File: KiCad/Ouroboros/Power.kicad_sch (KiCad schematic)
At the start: 8 parts, among them J2 Jack-DC, U1 Opamp_Quad, U3 LM78L05_TO92

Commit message: Updating schematic
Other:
- note added: "DC IN"
- note added: "[4] Power"
- moved on the sheet: C4, C5, C6, C7, J2, U3

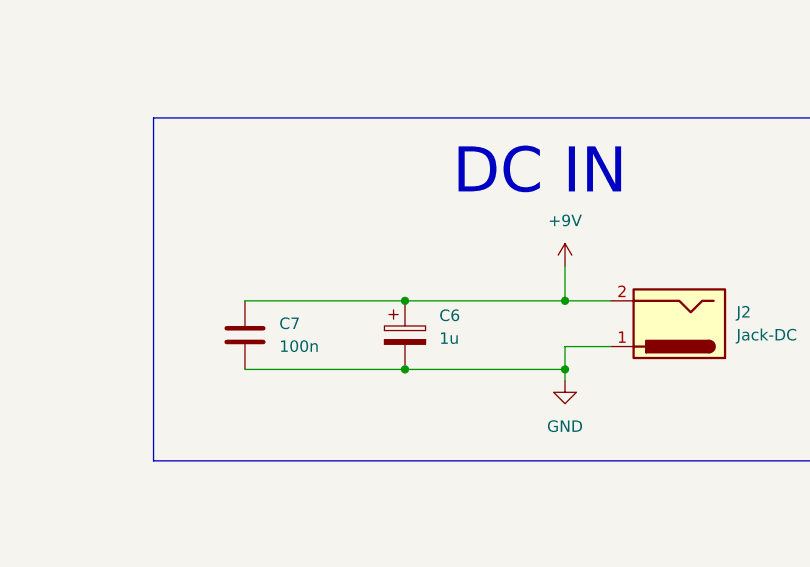
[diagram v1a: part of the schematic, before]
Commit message: Linking nets
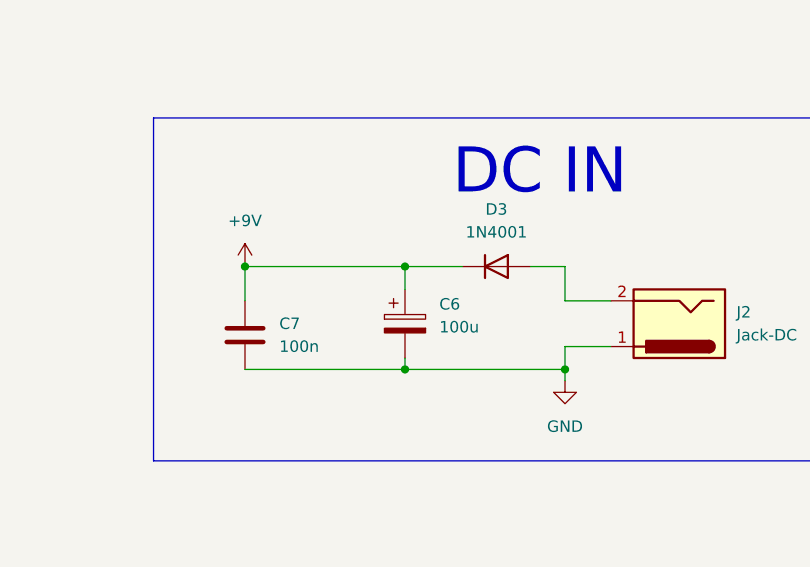
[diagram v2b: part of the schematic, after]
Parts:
- added D3: 1N4001, Diode_THT:D_DO-41_SOD81_P10.16mm_Horizontal, symbol Diode:1N4001
- C6: value 1u -> 100u
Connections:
- net +9V: now also D3.1 (K); no longer J2.2
- new net: D3.2 (A), J2.2
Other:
- moved on the sheet: C6
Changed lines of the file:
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@@
 	)
 	(junction
-		(at 134.62 63.5)
+		(at 116.84 59.69)
 		(diameter 0)
 		(color 0 0 0 0)
@@
 	)
 	(junction
-		(at 152.4 63.5)
-		(diameter 0)
-		(color 0 0 0 0)
-	)
-	(junction
 		(at 128.27 125.73)
 		(diameter 0)
@@
 		(color 0 0 0 0)
 	)
+	(junction
+		(at 134.62 59.69)
+		(diameter 0)
+		(color 0 0 0 0)
+	)
 	(polyline
 		(pts
@@
 	(wire
 		(pts
+			(xy 134.62 59.69) (xy 134.62 62.23)
+		)
+		(stroke
+			(width 0)
+			(type default)
+		)
+	)
+	(wire
+		(pts
 			(xy 54.61 93.98) (xy 54.61 99.06)
 		)
@@
 		)
 	)
+	(wire
+		(pts
+			(xy 148.59 59.69) (xy 152.4 59.69)
+		)
+		(stroke
+			(width 0)
+			(type default)
+		)
+	)
 	(polyline
 		(pts
@@
 	(wire
 		(pts
-			(xy 134.62 63.5) (xy 152.4 63.5)
-		)
-		(stroke
-			(width 0)
-			(type default)
-		)
-	)
-	(wire
-		(pts
 			(xy 74.93 99.06) (xy 74.93 101.6)
 		)
@@
 	(wire
 		(pts
+			(xy 134.62 69.85) (xy 134.62 71.12)
+		)
+		(stroke
+			(width 0)
+			(type default)
+		)
+	)
+	(wire
+		(pts
 			(xy 152.4 71.12) (xy 152.4 68.58)
 		)
@@
 		)
 	)
+	(wire
+		(pts
+			(xy 134.62 71.12) (xy 152.4 71.12)
+		)
+		(stroke
+			(width 0)
+			(type default)
+		)
+	)
 	(polyline
 		(pts
@@
 	(wire
 		(pts
+			(xy 134.62 59.69) (xy 140.97 59.69)
+		)
+		(stroke
+			(width 0)
+			(type default)
+		)
+	)
+	(wire
+		(pts
 			(xy 152.4 125.73) (xy 167.64 125.73)
 		)
@@
 	(wire
 		(pts
+			(xy 116.84 59.69) (xy 116.84 63.5)
+		)
+		(stroke
+			(width 0)
+			(type default)
+		)
+	)
+	(wire
+		(pts
 			(xy 128.27 125.73) (xy 137.16 125.73)
 		)
@@
 	(wire
 		(pts
-			(xy 134.62 71.12) (xy 152.4 71.12)
-		)
-		(stroke
-			(width 0)
-			(type default)
-		)
-	)
-	(wire
-		(pts
-			(xy 116.84 63.5) (xy 134.62 63.5)
+			(xy 116.84 59.69) (xy 134.62 59.69)
 		)
 		(stroke
@@
 	(symbol
 		(lib_id "Device:C_Polarized")
-		(at 134.62 67.31 0)
+		(at 134.62 66.04 0)
 		(unit 1)
 		(exclude_from_sim no)
@@
 		(fields_autoplaced yes)
 		(property "Reference" "C6"
-			(at 138.43 65.1509 0)
+			(at 138.43 63.8809 0)
 			(effects
 				(font
@@
 			)
 		)
-		(property "Value" "1u"
-			(at 138.43 67.6909 0)
+		(property "Value" "100u"
+			(at 138.43 66.4209 0)
 			(effects
 				(font
@@
 		)
 		(property "Footprint" ""
-			(at 135.5852 71.12 0)
+			(at 135.5852 69.85 0)
 			(effects
 				(font
@@
 		)
 		(property "Datasheet" "~"
-			(at 134.62 67.31 0)
+			(at 134.62 66.04 0)
 			(effects
 				(font
@@
 		)
 		(property "Description" "Polarized capacitor"
-			(at 134.62 67.31 0)
+			(at 134.62 66.04 0)
 			(effects
 				(font
@@
 	(symbol
 		(lib_id "power:+9V")
-		(at 152.4 59.69 0)
+		(at 116.84 59.69 0)
 		(unit 1)
 		(exclude_from_sim no)
@@
 		(fields_autoplaced yes)
 		(property "Reference" "#PWR08"
-			(at 152.4 63.5 0)
+			(at 116.84 63.5 0)
 			(effects
 				(font
@@
 		)
 		(property "Value" "+9V"
-			(at 152.4 54.61 0)
+			(at 116.84 54.61 0)
 			(effects
 				(font
@@
 		)
 		(property "Footprint" ""
-			(at 152.4 59.69 0)
+			(at 116.84 59.69 0)
 			(effects
 				(font
@@
 		)
 		(property "Datasheet" ""
-			(at 152.4 59.69 0)
+			(at 116.84 59.69 0)
 			(effects
 				(font
@@
 		)
 		(property "Description" "Power symbol creates a global label with name \"+9V\""
-			(at 152.4 59.69 0)
+			(at 116.84 59.69 0)
 			(effects
 				(font
@@
 					(unit 1)
 				)
+			)
+		)
+	)
+	(symbol
+		(lib_id "Diode:1N4001")
+		(at 144.78 59.69 0)
+		(unit 1)
+		(exclude_from_sim no)
+		(in_bom yes)
+		(on_board yes)
+		(dnp no)
+		(fields_autoplaced yes)
+		(property "Reference" "D3"
+			(at 144.78 53.34 0)
+			(effects
+				(font
+					(size 1.27 1.27)
+				)
+			)
+		)
+		(property "Value" "1N4001"
+			(at 144.78 55.88 0)
+			(effects
+				(font
+					(size 1.27 1.27)
+				)
+			)
+		)
+		(property "Footprint" "Diode_THT:D_DO-41_SOD81_P10.16mm_Horizontal"
+			(at 144.78 59.69 0)
+			(effects
+				(font
+					(size 1.27 1.27)
+				)
+				(hide yes)
+			)
+		)
+		(property "Datasheet" "http://www.vishay.com/docs/88503/1n4001.pdf"
+			(at 144.78 59.69 0)
+			(effects
+				(font
+					(size 1.27 1.27)
+				)
+				(hide yes)
+			)
+		)
+		(property "Description" "50V 1A General Purpose Rectifier Diode, DO-41"
+			(at 144.78 59.69 0)
+			(effects
+				(font
+					(size 1.27 1.27)
+				)
+				(hide yes)
+			)
+		)
+		(property "Sim.Device" "D"
+			(at 144.78 59.69 0)
+			(effects
+				(font
+					(size 1.27 1.27)
+				)
+				(hide yes)
+			)
+		)
+		(property "Sim.Pins" "1=K 2=A"
+			(at 144.78 59.69 0)
+			(effects
+				(font
+					(size 1.27 1.27)
+				)
+				(hide yes)
+			)
+		)
+		(pin "2"
+		)
+		(pin "1"
+		)
+		(instances
+			(project ""
+				(path "/a2662f7c-8239-40ad-828c-dd886b1cb258/62d72753-1043-42a5-8194-984b7e294543"
+					(reference "D3")
+					(unit 1)
+				)

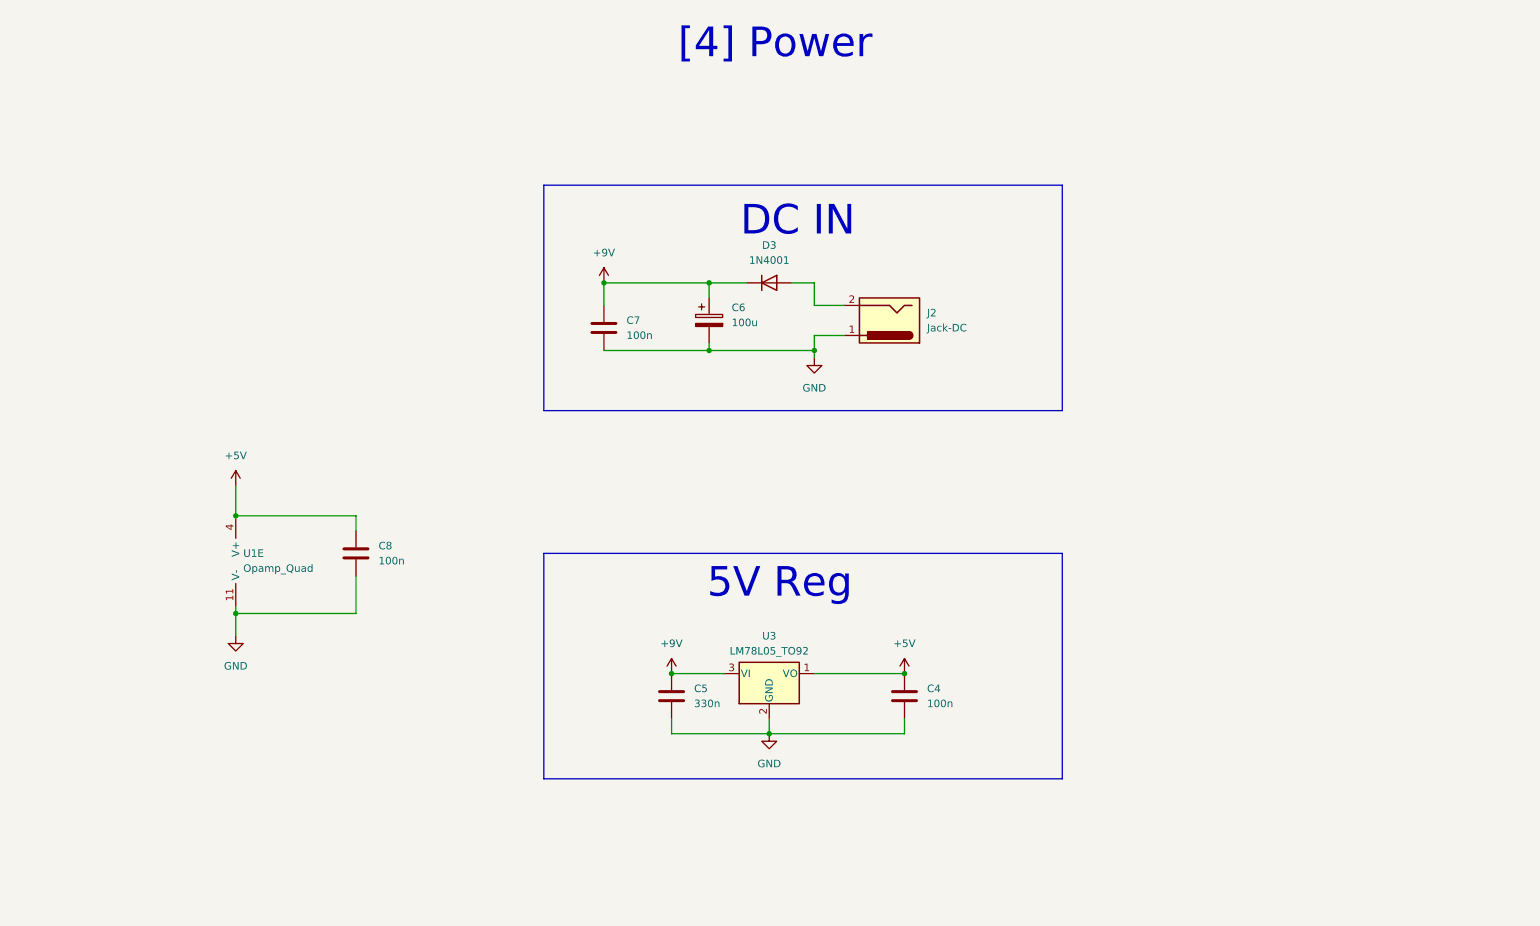
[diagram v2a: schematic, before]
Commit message: Updated schematic, started PCB
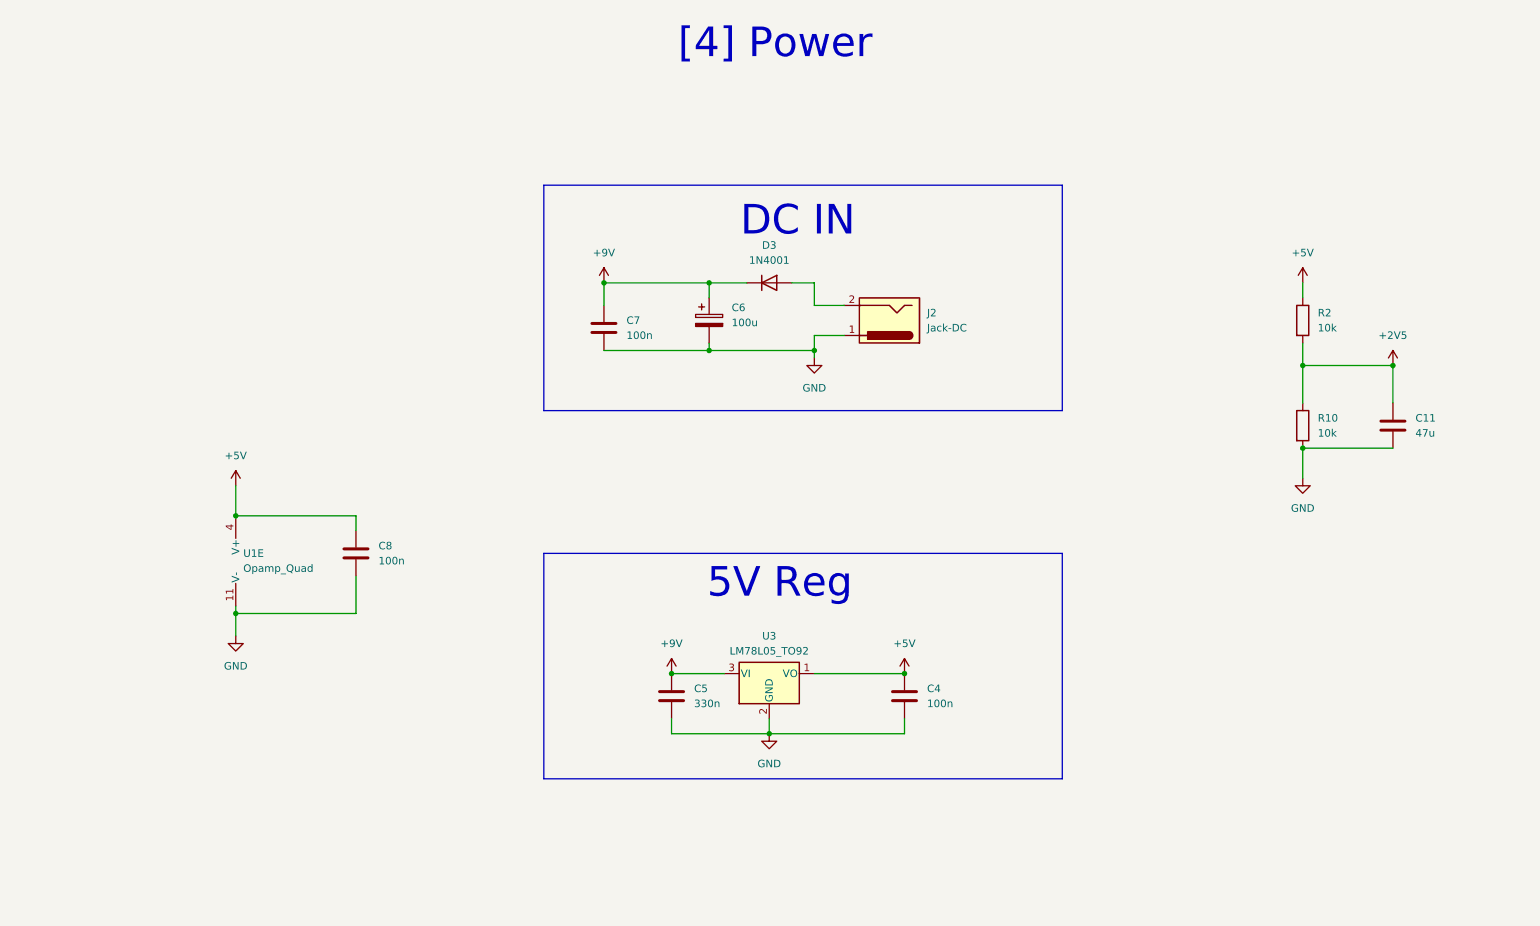
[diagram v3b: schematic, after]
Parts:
- added C11: 47u, Capacitor_THT:C_Rect_L7.0mm_W3.5mm_P5.00mm, symbol Device:C
- added R10, R2: 10k, Resistor_THT:R_Axial_DIN0207_L6.3mm_D2.5mm_P10.16mm_Horizontal, symbol Device:R
- C4, C5, C7, C8: footprint (none) -> Capacitor_THT:C_Rect_L7.0mm_W3.5mm_P5.00mm
- C6: footprint (none) -> Capacitor_THT:CP_Radial_D5.0mm_P2.50mm
- J2: footprint (none) -> Connector_BarrelJack:BarrelJack_CUI_PJ-063AH_Horizontal_CircularHoles
- U1: footprint (none) -> Package_DIP:DIP-14_W7.62mm_Socket; symbol Device:Opamp_Quad -> Amplifier_Operational:TL074
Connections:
- net +5V: now also R2.1
- net GND: now also C11.2, R10.2
- new net +2V5: C11.1, R10.1, R2.2

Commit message: PCB Finished
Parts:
- J2: symbol Connector:Jack-DC -> Connector:Barrel_Jack_MountingPin
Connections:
- net GND: now also J2.MP (MountPin)
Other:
- note added: "2.5V Rail"
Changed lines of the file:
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@@
+		)
+	)
+	(polyline
+		(pts
+			(xy 223.52 102.87) (xy 273.05 102.87)
+		)
+		(stroke
+			(width 0)
+			(type default)
 		)
 	)
@@
 		)
 	)
+	(polyline
+		(pts
+			(xy 223.52 49.53) (xy 273.05 49.53)
+		)
+		(stroke
+			(width 0)
+			(type default)
+		)
+	)
 	(wire
 		(pts
@@
 		)
 	)
+	(polyline
+		(pts
+			(xy 223.52 49.53) (xy 223.52 102.87)
+		)
+		(stroke
+			(width 0)
+			(type default)
+		)
+	)
 	(wire
 		(pts
@@
 		)
 	)
+	(polyline
+		(pts
+			(xy 273.05 102.87) (xy 273.05 49.53)
+		)
+		(stroke
+			(width 0)
+			(type default)
+		)
+	)
 	(wire
 		(pts
@@
 		(pts
 			(xy 128.27 133.35) (xy 128.27 135.89)
+		)
+		(stroke
+			(width 0)
+			(type default)
+		)
+	)
+	(wire
+		(pts
+			(xy 165.1 58.42) (xy 168.91 58.42)
 		)
 		(stroke
@@
 		)
 	)
+	(text "2.5V Rail\n"
+		(exclude_from_sim no)
+		(at 251.968 54.356 0)
+		(effects
+			(font
+				(size 3 3)
+			)
+		)
+	)
 	(symbol
 		(lib_id "Device:C")
@@
 	)
 	(symbol
-		(lib_id "Connector:Jack-DC")
+		(lib_id "Connector:Barrel_Jack_MountingPin")
 		(at 165.1 66.04 180)
 		(unit 1)
@@
 		(fields_autoplaced yes)
 		(property "Reference" "J2"
-			(at 171.45 64.7699 0)
+			(at 171.45 64.4143 0)
 			(effects
 				(font
@@
 		)
 		(property "Value" "Jack-DC"
-			(at 171.45 67.3099 0)
+			(at 171.45 66.9543 0)
 			(effects
 				(font
@@
 			)
 		)
-		(property "Description" "DC Barrel Jack"
+		(property "Description" "DC Barrel Jack with a mounting pin"
 			(at 165.1 66.04 0)
 			(effects
@@
 		)
 		(pin "1"
+		)
+		(pin "MP"
 		)
 		(instances
@@
 				)
 			)
+		)
+	)
+	(symbol
+		(lib_id "power:GND")
+		(at 168.91 58.42 90)
+		(unit 1)
+		(exclude_from_sim no)
+		(in_bom yes)
+		(on_board yes)
+		(dnp no)
+		(fields_autoplaced yes)
+		(property "Reference" "#PWR050"
+			(at 175.26 58.42 0)
+			(effects
+				(font
+					(size 1.27 1.27)
+				)
+				(hide yes)
+			)
+		)
+		(property "Value" "GND"
+			(at 172.72 58.4199 90)
+			(effects
+				(font
+					(size 1.27 1.27)
+				)
+				(justify right)
+			)
+		)
+		(property "Footprint" ""
+			(at 168.91 58.42 0)
+			(effects
+				(font
+					(size 1.27 1.27)
+				)
+				(hide yes)
+			)
+		)
+		(property "Datasheet" ""
+			(at 168.91 58.42 0)
+			(effects
+				(font
+					(size 1.27 1.27)
+				)
+				(hide yes)
+			)
+		)
+		(property "Description" "Power symbol creates a global label with name \"GND\" , ground"
+			(at 168.91 58.42 0)
+			(effects
+				(font
+					(size 1.27 1.27)
+				)
+				(hide yes)
+			)
+		)
+		(pin "1"
+		)
+		(instances
+			(project "Ouroboros"
+				(path "/a2662f7c-8239-40ad-828c-dd886b1cb258/62d72753-1043-42a5-8194-984b7e294543"
+					(reference "#PWR050")
+					(unit 1)
+				)
+			)

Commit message: Dev Board complete
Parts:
- added C24: 100n, Capacitor_THT:C_Rect_L7.0mm_W3.5mm_P5.00mm, symbol Device:C
- added U2: Opamp_Dual, Package_DIP:DIP-8_W7.62mm_Socket, symbol Device:Opamp_Dual
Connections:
- net +5V: now also C24.1, U2.8 (V+)
- net GND: now also C24.2, U2.4 (V-)
